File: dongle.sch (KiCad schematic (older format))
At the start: 88 parts, among them J1 AudioJack2_Ground_Switch, J2 AudioJack2_Ground_Switch, J3 AudioJack2_Ground_Switch, J4 AudioJack2_Ground_Switch, J5 AudioJack2_Ground_Switch, P1 Digital, P2 CONN_01X01, P3 CONN_01X01, P4 Analog, P5 CONN_01X01, P6 CONN_01X01, Q1 MMBT3904, Q10 MMBT3904, Q11 MMBT3904, Q12 MMBT3904, Q13 MMBT3904, Q14 MMBT3904, Q15 MMBT3904, Q16 MMBT3904, Q17 MMBT3904, Q18 MMBT3904, Q19 MMBT3904, Q2 MMBT3904, Q20 MMBT3904, Q3 MMBT3904, Q4 MMBT3904, Q5 MMBT3904, Q6 MMBT3904, Q7 MMBT3904, Q8 MMBT3904, Q9 MMBT3904, SW1 SW_DIP_x01

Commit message: Change the footprints on the LED's to indicate which pad is for the cathode so that they can be soldered more easily.
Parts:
- D1, D10, D11, D12, D2, D3, D4, D5, D6, D7, D8, D9: footprint LED_SMD:LED_0805_2012Metric -> LED_SMD:LED_0805_2012Metric_Pad1.15x1.40mm_HandSolder
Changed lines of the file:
@@
 F 0 "D3" H 12750 12850 50  0000 C CNN
 F 1 "RED" H 12600 12850 50  0000 C CNN
-F 2 "LED_SMD:LED_0805_2012Metric" H 12600 12950 50  0001 C CNN
+F 2 "LED_SMD:LED_0805_2012Metric_Pad1.15x1.40mm_HandSolder" H 12600 12950 50  0001 C CNN
 F 3 "~" H 12600 12950 50  0001 C CNN
 	1    12600 12950
@@
 F 0 "D5" H 13600 12750 50  0000 C CNN
 F 1 "BLUE" H 13550 12850 50  0000 C CNN
-F 2 "LED_SMD:LED_0805_2012Metric" H 13550 12950 50  0001 C CNN
+F 2 "LED_SMD:LED_0805_2012Metric_Pad1.15x1.40mm_HandSolder" H 13550 12950 50  0001 C CNN
 F 3 "~" H 13550 12950 50  0001 C CNN
 	1    13550 12950
@@
 F 0 "D1" H 10950 13450 50  0000 C CNN
 F 1 "YELLOW" H 10700 13450 50  0000 C CNN
-F 2 "LED_SMD:LED_0805_2012Metric" H 10900 13600 50  0001 C CNN
+F 2 "LED_SMD:LED_0805_2012Metric_Pad1.15x1.40mm_HandSolder" H 10900 13600 50  0001 C CNN
 F 3 "~" H 10900 13600 50  0001 C CNN
 	1    10900 13600
@@
 F 0 "D2" H 11200 16500 50  0000 C CNN
 F 1 "YELLOW" H 10950 16500 50  0000 C CNN
-F 2 "LED_SMD:LED_0805_2012Metric" H 11000 16600 50  0001 C CNN
+F 2 "LED_SMD:LED_0805_2012Metric_Pad1.15x1.40mm_HandSolder" H 11000 16600 50  0001 C CNN
 F 3 "~" H 11000 16600 50  0001 C CNN
 	1    11000 16600
@@
 F 0 "D4" H 12900 15750 50  0000 C CNN
 F 1 "RED" H 12850 15850 50  0000 C CNN
-F 2 "LED_SMD:LED_0805_2012Metric" H 12900 15950 50  0001 C CNN
+F 2 "LED_SMD:LED_0805_2012Metric_Pad1.15x1.40mm_HandSolder" H 12900 15950 50  0001 C CNN
 F 3 "~" H 12900 15950 50  0001 C CNN
 	1    12900 15950
@@
 F 0 "D6" H 13450 15300 50  0000 C CNN
 F 1 "BLUE" H 13400 15400 50  0000 C CNN
-F 2 "LED_SMD:LED_0805_2012Metric" H 13600 15550 50  0001 C CNN
+F 2 "LED_SMD:LED_0805_2012Metric_Pad1.15x1.40mm_HandSolder" H 13600 15550 50  0001 C CNN
 F 3 "~" H 13600 15550 50  0001 C CNN
 	1    13600 15550
@@
 F 0 "D10" H 20750 12800 50  0000 C CNN
 F 1 "RED" H 20700 12900 50  0000 C CNN
-F 2 "LED_SMD:LED_0805_2012Metric" H 20700 13000 50  0001 C CNN
+F 2 "LED_SMD:LED_0805_2012Metric_Pad1.15x1.40mm_HandSolder" H 20700 13000 50  0001 C CNN
 F 3 "~" H 20700 13000 50  0001 C CNN
 	1    20700 13000
@@
 F 0 "D12" H 23050 13150 50  0000 C CNN
 F 1 "YELLOW" H 23000 13250 50  0000 C CNN
-F 2 "LED_SMD:LED_0805_2012Metric" H 23000 13350 50  0001 C CNN
+F 2 "LED_SMD:LED_0805_2012Metric_Pad1.15x1.40mm_HandSolder" H 23000 13350 50  0001 C CNN
 F 3 "~" H 23000 13350 50  0001 C CNN
 	1    23000 13350
@@
 F 0 "D8" H 18500 12500 50  0000 C CNN
 F 1 "BLUE" H 18450 12600 50  0000 C CNN
-F 2 "LED_SMD:LED_0805_2012Metric" H 18450 12700 50  0001 C CNN
+F 2 "LED_SMD:LED_0805_2012Metric_Pad1.15x1.40mm_HandSolder" H 18450 12700 50  0001 C CNN
 F 3 "~" H 18450 12700 50  0001 C CNN
 	1    18450 12700
@@
 F 0 "D7" H 18300 15350 50  0000 C CNN
 F 1 "BLUE" H 18250 15450 50  0000 C CNN
-F 2 "LED_SMD:LED_0805_2012Metric" H 18250 15550 50  0001 C CNN
+F 2 "LED_SMD:LED_0805_2012Metric_Pad1.15x1.40mm_HandSolder" H 18250 15550 50  0001 C CNN
 F 3 "~" H 18250 15550 50  0001 C CNN
 	1    18250 15550
@@
 F 0 "D11" H 22800 16450 50  0000 C CNN
 F 1 "YELLOW" H 22750 16550 50  0000 C CNN
-F 2 "LED_SMD:LED_0805_2012Metric" H 22750 16650 50  0001 C CNN
+F 2 "LED_SMD:LED_0805_2012Metric_Pad1.15x1.40mm_HandSolder" H 22750 16650 50  0001 C CNN
 F 3 "~" H 22750 16650 50  0001 C CNN
 	1    22750 16650
@@
 F 0 "D9" H 20450 16100 50  0000 C CNN
 F 1 "RED" H 20400 16200 50  0000 C CNN
-F 2 "LED_SMD:LED_0805_2012Metric" H 20400 16300 50  0001 C CNN
+F 2 "LED_SMD:LED_0805_2012Metric_Pad1.15x1.40mm_HandSolder" H 20400 16300 50  0001 C CNN
 F 3 "~" H 20400 16300 50  0001 C CNN
 	1    20400 16300

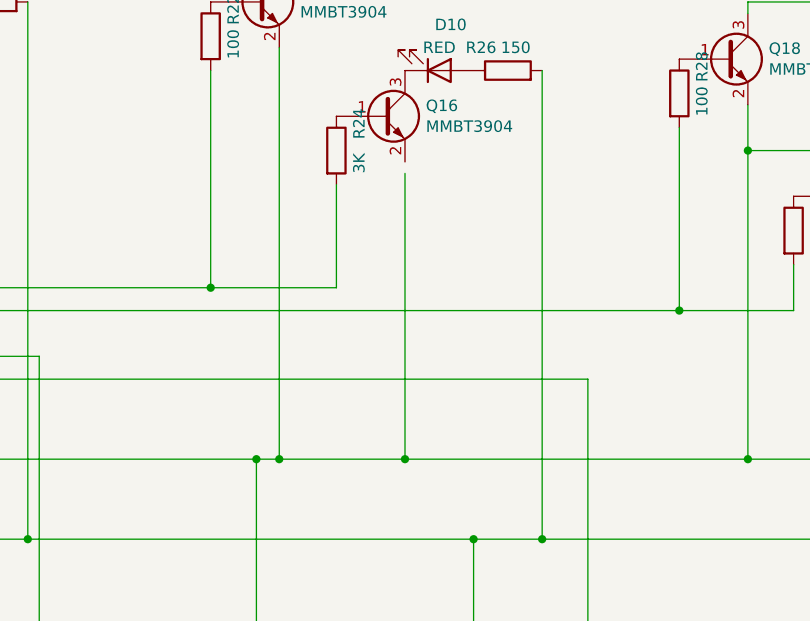
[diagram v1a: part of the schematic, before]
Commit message: Fix an error in the schematic and update the PC board layout.
The emitter of Q16 needs to be grounded or port 3's red LED doesn't work.
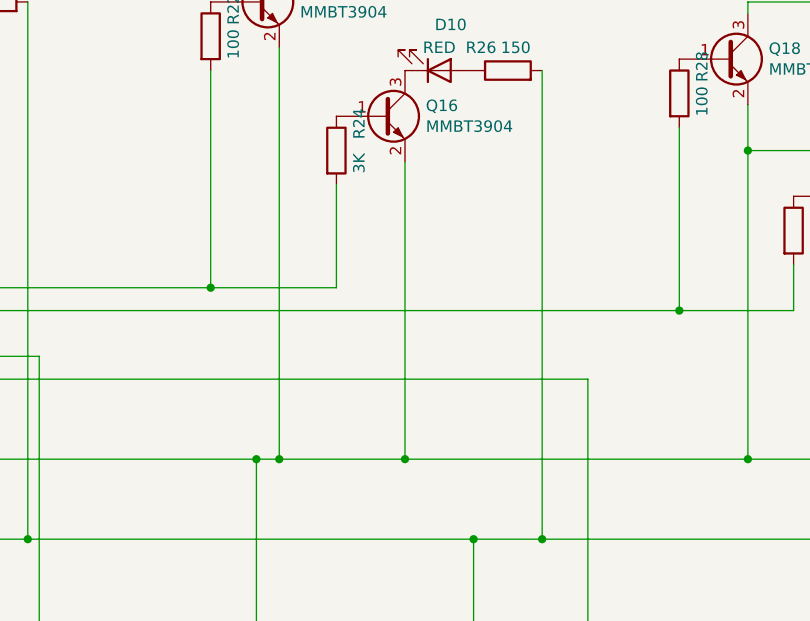
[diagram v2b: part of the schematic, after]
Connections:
- net GND: now also Q16.2 (E)
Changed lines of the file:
@@
 	22550 13750 22550 14700
 Connection ~ 22550 14700
-Wire Wire Line
-	20550 13450 20550 14700
 Connection ~ 20550 14700
 Wire Wire Line
@@
 Wire Wire Line
 	16850 13300 16850 13550
+Wire Wire Line
+	20550 13400 20550 14700
 $EndSCHEMATC

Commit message: While I'm at it, I can also fix the footprint of the buzzer, which doesn't match the parts I actually have, and fix another issue when I ran a DRC
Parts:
- LS1: footprint Buzzer_Beeper:Buzzer_D14mm_H7mm_P10mm -> Buzzer_Beeper:Buzzer_15x7.5RM7.6
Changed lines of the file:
@@
 F 0 "LS1" V 14712 12170 50  0000 R CNN
 F 1 "Speaker_Crystal" V 14621 12170 50  0000 R CNN
-F 2 "Buzzer_Beeper:Buzzer_D14mm_H7mm_P10mm" H 14665 12400 50  0001 C CNN
+F 2 "Buzzer_Beeper:Buzzer_15x7.5RM7.6" H 14665 12400 50  0001 C CNN
 F 3 "~" H 14665 12400 50  0001 C CNN
 	1    14700 12450
